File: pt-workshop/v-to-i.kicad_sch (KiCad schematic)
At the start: 12 parts, among them Q301 NST65011, U301 TL972

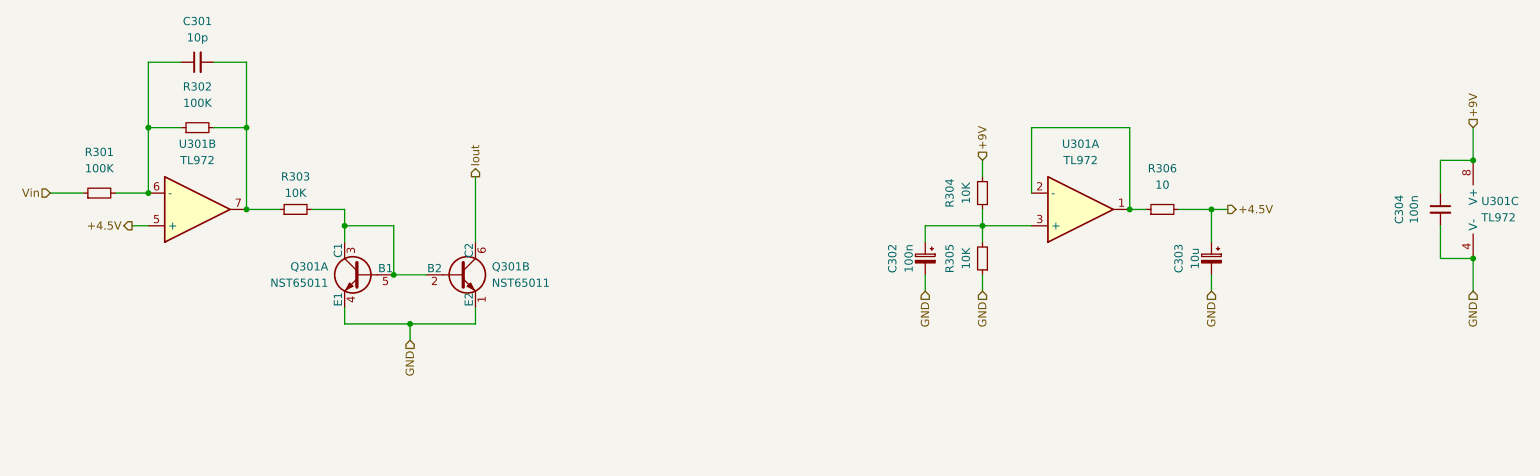
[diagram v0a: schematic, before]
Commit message: 10 pin socket
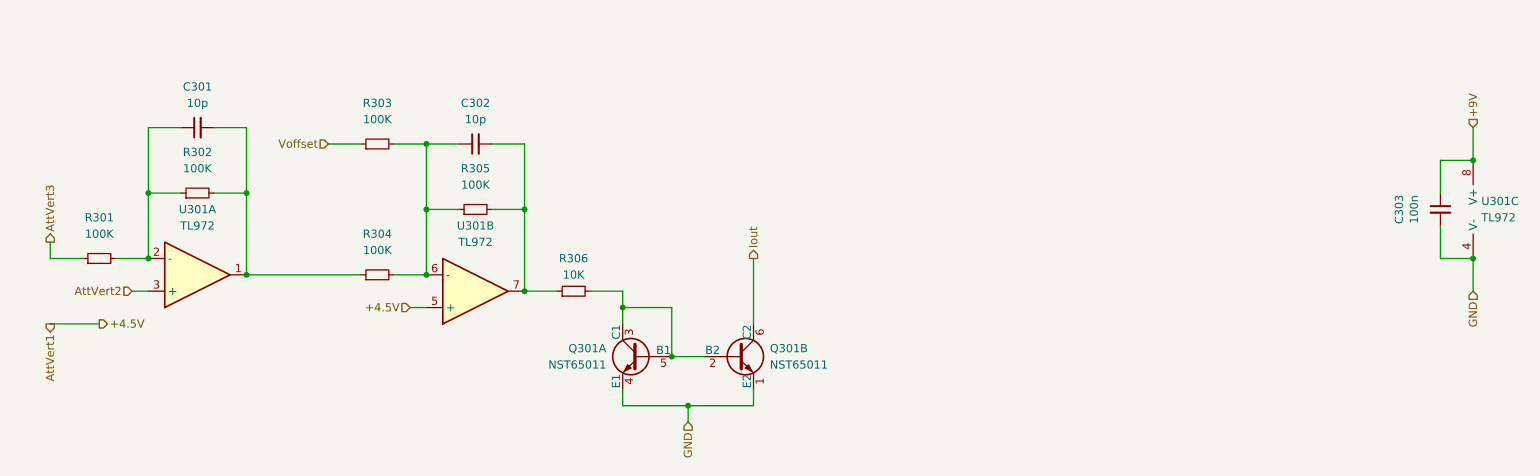
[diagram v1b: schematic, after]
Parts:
- removed C302: 100n, Capacitor_SMD:CP_Elec_4x5.4, symbol Device:C_Polarized_Small
- removed C303: 10u, Capacitor_SMD:CP_Elec_5x5.4, symbol Device:C_Polarized_Small
- removed R305: 10K, Resistor_SMD:R_0603_1608Metric_Pad0.98x0.95mm_HandSolder, symbol Device:R_Small
- removed R306: 10, Resistor_SMD:R_0603_1608Metric_Pad0.98x0.95mm_HandSolder, symbol Device:R_Small
- added C301: 10p, Capacitor_SMD:C_0603_1608Metric_Pad1.08x0.95mm_HandSolder, symbol Device:C_Small
- added R301, R302: 100K, Resistor_SMD:R_0603_1608Metric_Pad0.98x0.95mm_HandSolder, symbol Device:R_Small
- R304: value 10K -> 100K; LCSC C98220 -> (none); Mouser 603-RT0603DRE1010KL -> (none)
- renumbered C301 to C302, C304 to C303, R301 to R303, R302 to R305, R303 to R306
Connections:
- net +9V: no longer R304.2
- net at U301.2 (-): now also C301.1, R301.2, R302.1; no longer U301.1
- net at C302.1, R303.2, R305.1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: now also R304.2
- net at R304.1: now also U301.1, C301.2, R302.2; no longer U301.3 (+)
- net Vin renamed Voffset
- new net AttVert2: U301.3 (+)
- new net AttVert3: R301.1
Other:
- moved on the sheet: C302, Q301A, Q301B, R303, R305, R306, U301A, U301B

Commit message: Mapped components
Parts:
- added TP1: Vatt, TestPoint:TestPoint_Pad_1.5x1.5mm, symbol Connector:TestPoint
- added TP2: Vd, TestPoint:TestPoint_Pad_1.5x1.5mm, symbol Connector:TestPoint
- C301, C302: LCSC (none) -> C91367
- C303: LCSC C497032 -> C57112
- R301, R302, R303, R304, R305: LCSC (none) -> C25803
- R306: LCSC C98220 -> C25804
- U301: LCSC (none) -> C46127
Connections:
- net at C302.2, R305.2, R306.1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: now also TP2.1
- net at C301.2, R302.2, R304.1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: now also TP1.1
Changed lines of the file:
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@@
   (junction (at 91.44 53.34) (diameter 0) (color 0 0 0 0)
   )
+  (junction (at 71.12 53.34) (diameter 0) (color 0 0 0 0)
+  )
   (junction (at 48.26 40.64) (diameter 0) (color 0 0 0 0)
   )
@@
     (stroke (width 0) (type default) (color 0 0 0 0))
   )
+  (wire (pts (xy 71.12 53.34) (xy 81.28 53.34))
+    (stroke (width 0) (type default) (color 0 0 0 0))
+  )
   (wire (pts (xy 91.44 33.02) (xy 91.44 43.18))
     (stroke (width 0) (type default) (color 0 0 0 0))
@@
     (stroke (width 0) (type default) (color 0 0 0 0))
   )
-  (wire (pts (xy 63.5 53.34) (xy 81.28 53.34))
+  (wire (pts (xy 63.5 53.34) (xy 71.12 53.34))
     (stroke (width 0) (type default) (color 0 0 0 0))
   )
@@
     (stroke (width 0) (type default) (color 0 0 0 0))
   )
+  (wire (pts (xy 71.12 53.34) (xy 71.12 59.69))
+    (stroke (width 0) (type default) (color 0 0 0 0))
+  )
   (wire (pts (xy 106.68 55.88) (xy 111.76 55.88))
+    (stroke (width 0) (type default) (color 0 0 0 0))
+  )
+  (wire (pts (xy 106.68 55.88) (xy 106.68 58.42))
     (stroke (width 0) (type default) (color 0 0 0 0))
   )
@@
       (effects (font (size 1.27 1.27)) hide)
     )
-    (property "LCSC" "C497032" (id 4) (at 248.92 43.18 0)
+    (property "LCSC" "C57112" (id 4) (at 248.92 43.18 0)
       (effects (font (size 1.27 1.27)) hide)
     )
@@
       (effects (font (size 1.27 1.27)) hide)
     )
+    (property "LCSC" "C25803" (id 4) (at 40.64 50.8 0)
+      (effects (font (size 1.27 1.27)) hide)
+    )
     (pin "1")
     (pin "2")
@@
     )
     (property "Datasheet" "~" (id 3) (at 256.54 43.18 0)
+      (effects (font (size 1.27 1.27)) hide)
+    )
+    (property "LCSC" "C46127" (id 4) (at 256.54 43.18 0)
       (effects (font (size 1.27 1.27)) hide)
     )
@@
       (effects (font (size 1.27 1.27)) hide)
     )
-    (pin "1")
-    (pin "2")
+    (property "LCSC" "C91367" (id 4) (at 99.06 33.02 0)
+      (effects (font (size 1.27 1.27)) hide)
+    )
+    (pin "1")
+    (pin "2")
+  )
+  (symbol (lib_id "Connector:TestPoint") (at 71.12 59.69 180) (unit 1)
+    (in_bom yes) (on_board yes) (fields_autoplaced)
+    (property "Reference" "TP1" (id 0) (at 73.66 61.7219 0)
+      (effects (font (size 1.27 1.27)) (justify right))
+    )
+    (property "Value" "Vatt" (id 1) (at 73.66 64.2619 0)
+      (effects (font (size 1.27 1.27)) (justify right))
+    )
+    (property "Footprint" "TestPoint:TestPoint_Pad_1.5x1.5mm" (id 2) (at 66.04 59.69 0)
+      (effects (font (size 1.27 1.27)) hide)
+    )
+    (property "Datasheet" "~" (id 3) (at 66.04 59.69 0)
+      (effects (font (size 1.27 1.27)) hide)
+    )
+    (pin "1")
   )
   (symbol (lib_id "Device:R_Small") (at 55.88 40.64 90) (unit 1)
@@
       (effects (font (size 1.27 1.27)) hide)
     )
+    (property "LCSC" "C25803" (id 4) (at 55.88 40.64 0)
+      (effects (font (size 1.27 1.27)) hide)
+    )
     (pin "1")
     (pin "2")
@@
     )
     (property "Datasheet" "~" (id 3) (at 83.82 53.34 0)
+      (effects (font (size 1.27 1.27)) hide)
+    )
+    (property "LCSC" "C25803" (id 4) (at 83.82 53.34 0)
       (effects (font (size 1.27 1.27)) hide)
     )
@@
       (effects (font (size 1.27 1.27)) hide)
     )
-    (property "LCSC" "C98220" (id 4) (at 114.3 55.88 0)
+    (property "LCSC" "C25804" (id 4) (at 114.3 55.88 0)
       (effects (font (size 1.27 1.27)) hide)
     )
@@
     )
     (property "Datasheet" "~" (id 3) (at 55.88 53.34 0)
+      (effects (font (size 1.27 1.27)) hide)
+    )
+    (property "LCSC" "C46127" (id 4) (at 55.88 53.34 0)
       (effects (font (size 1.27 1.27)) hide)
     )
@@
       (effects (font (size 1.27 1.27)) hide)
     )
+    (property "LCSC" "C46127" (id 4) (at 99.06 55.88 0)
+      (effects (font (size 1.27 1.27)) hide)
+    )
     (pin "1")
     (pin "2")
@@
       (effects (font (size 1.27 1.27)) hide)
     )
-    (pin "1")
-    (pin "2")
+    (property "LCSC" "C91367" (id 4) (at 55.88 30.48 0)
+      (effects (font (size 1.27 1.27)) hide)
+    )
+    (pin "1")
+    (pin "2")
+  )
+  (symbol (lib_id "Connector:TestPoint") (at 106.68 58.42 180) (unit 1)
+    (in_bom yes) (on_board yes) (fields_autoplaced)
+    (property "Reference" "TP2" (id 0) (at 109.22 60.4519 0)
+      (effects (font (size 1.27 1.27)) (justify right))
+    )
+    (property "Value" "Vd" (id 1) (at 109.22 62.9919 0)
+      (effects (font (size 1.27 1.27)) (justify right))
+    )
+    (property "Footprint" "TestPoint:TestPoint_Pad_1.5x1.5mm" (id 2) (at 101.6 58.42 0)
+      (effects (font (size 1.27 1.27)) hide)
+    )
+    (property "Datasheet" "~" (id 3) (at 101.6 58.42 0)
+      (effects (font (size 1.27 1.27)) hide)
+    )
+    (pin "1")
   )
   (symbol (lib_id "Device:R_Small") (at 99.06 43.18 90) (unit 1)
@@
       (effects (font (size 1.27 1.27)) hide)
     )
+    (property "LCSC" "C25803" (id 4) (at 99.06 43.18 0)
+      (effects (font (size 1.27 1.27)) hide)
+    )
     (pin "1")
     (pin "2")
@@
       (effects (font (size 1.27 1.27)) hide)
     )
+    (property "LCSC" "C25803" (id 4) (at 83.82 33.02 0)
+      (effects (font (size 1.27 1.27)) hide)
+    )

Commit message: v1rev1?
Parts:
- Q301: LCSC (none) -> C463185
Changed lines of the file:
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@@
+      (effects (font (size 1.27 1.27)) hide)
+    )
+    (property "LCSC" "C463185" (id 4) (at 124.46 66.04 0)
       (effects (font (size 1.27 1.27)) hide)
     )
@@
       (effects (font (size 1.27 1.27)) hide)
     )
+    (property "LCSC" "C463185" (id 4) (at 139.7 66.04 0)
+      (effects (font (size 1.27 1.27)) hide)
+    )

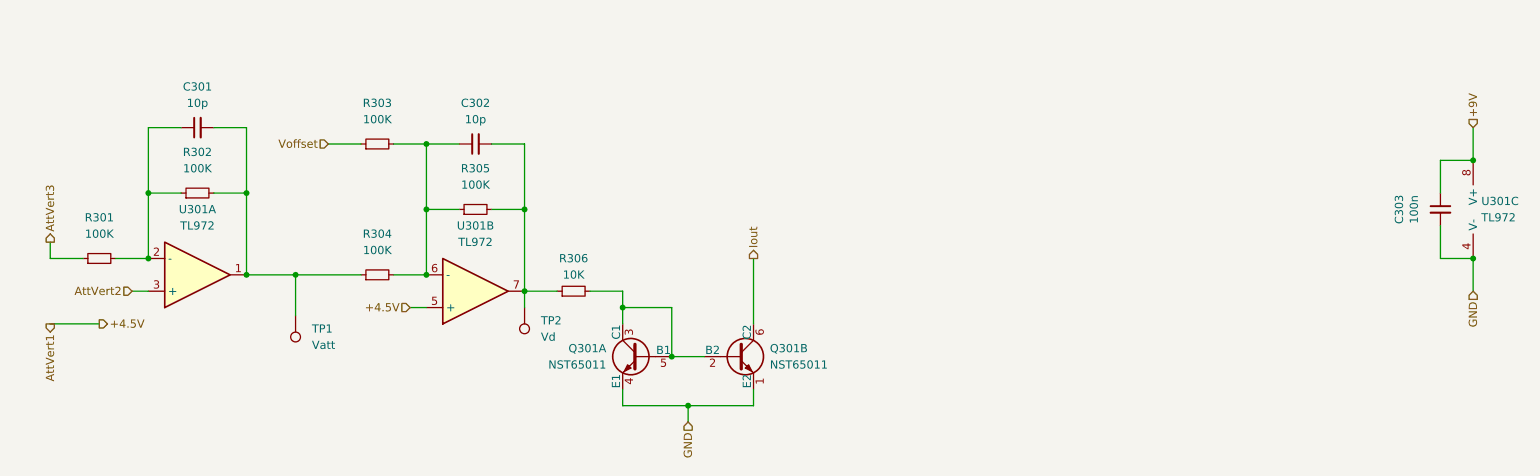
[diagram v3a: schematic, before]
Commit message: PTT without attverts
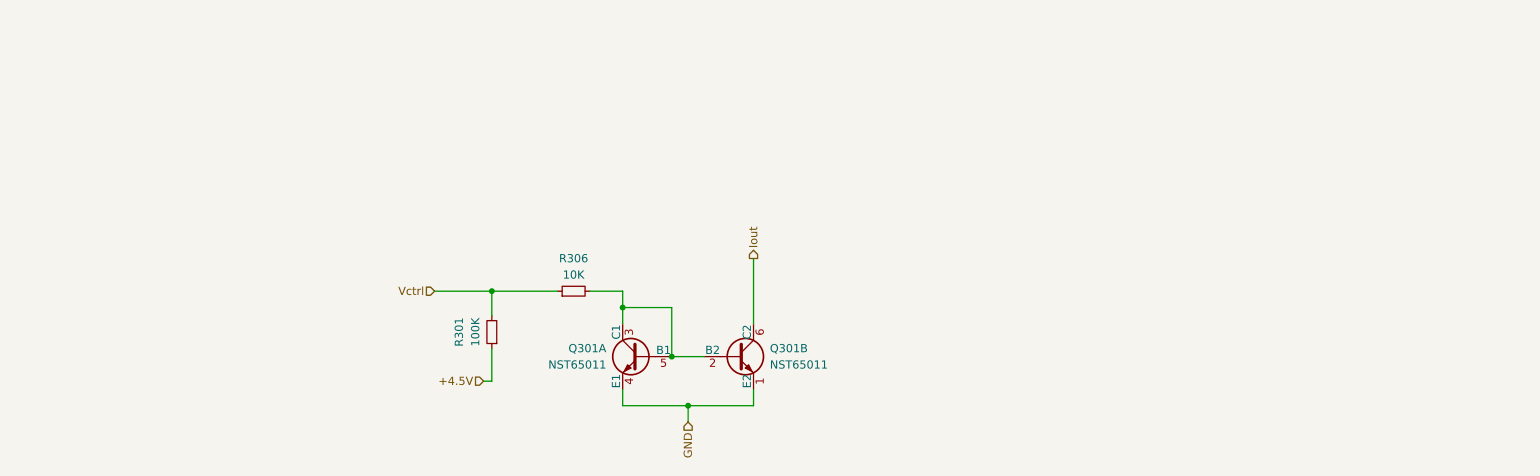
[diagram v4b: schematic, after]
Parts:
- removed C301, C302: 10p, Capacitor_SMD:C_0603_1608Metric_Pad1.08x0.95mm_HandSolder, symbol Device:C_Small
- removed C303: 100n, Capacitor_SMD:C_0603_1608Metric_Pad1.08x0.95mm_HandSolder, symbol Device:C_Small
- removed R302, R303, R304, R305: 100K, Resistor_SMD:R_0603_1608Metric_Pad0.98x0.95mm_HandSolder, symbol Device:R_Small
- removed TP1: Vatt, TestPoint:TestPoint_Pad_1.5x1.5mm, symbol Connector:TestPoint
- removed TP2: Vd, TestPoint:TestPoint_Pad_1.5x1.5mm, symbol Connector:TestPoint
- removed U301: TL972, Package_SO:SOIC-8_3.9x4.9mm_P1.27mm, symbol Device:Opamp_Dual
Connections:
- net AttVert3 is gone; now on net +4.5V: R301.1
- net Vctrl: now reaches R301.2
- net Vctrl: now also R306.1

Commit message: jlc
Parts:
- R306: Mouser 603-RT0603DRE1010KL -> (none)
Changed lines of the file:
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@@
       (effects (font (size 1.27 1.27)) hide)
     )
-    (property "Mouser" "603-RT0603DRE1010KL" (id 5) (at 114.3 55.88 0)
+    (property "Mouser" "" (id 5) (at 114.3 55.88 0)
       (effects (font (size 1.27 1.27)) hide)
     )

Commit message: PTT schem export
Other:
- company: (none) -> Pedal Markt
- title: (none) -> PTT
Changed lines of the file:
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@@
 (kicad_sch (version 20211123) (generator eeschema)
   (paper "A4")
+  (title_block
+    (title "PTT")
+    (date "2024-05-11")
+    (rev "v1rev2")
+    (company "Pedal Markt")
+    (comment 1 "Andrey Salomatin")
+  )
   (junction (at 101.6 55.88) (diameter 0) (color 0 0 0 0)
   )

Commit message: wip
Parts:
- Q301: value NST65011 -> MMDT3904; LCSC C463185 -> C41375125; LCSC v0 (none) -> C463185
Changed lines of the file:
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@@
     (title "PTT")
     (date "2024-05-11")
-    (rev "v1rev2")
+    (rev "v1rev3")
     (company "Pedal Markt")
     (comment 1 "Andrey Salomatin")
@@
       (effects (font (size 1.27 1.27)) (justify left))
     )
-    (property "Value" "NST65011" (id 1) (at 119.38 67.3099 0)
+    (property "Value" "MMDT3904" (id 1) (at 119.38 67.3099 0)
       (effects (font (size 1.27 1.27)) (justify left))
     )
@@
       (effects (font (size 1.27 1.27)) hide)
     )
-    (property "LCSC" "C463185" (id 4) (at 124.46 66.04 0)
+    (property "LCSC" "C41375125" (id 4) (at 124.46 66.04 0)
+      (effects (font (size 1.27 1.27)) hide)
+    )
+    (property "LCSC v0" "C463185" (id 5) (at 124.46 66.04 0)
       (effects (font (size 1.27 1.27)) hide)
     )
@@
       (effects (font (size 1.27 1.27)) (justify left))
     )
-    (property "Value" "NST65011" (id 1) (at 144.78 67.3099 0)
+    (property "Value" "MMDT3904" (id 1) (at 144.78 67.3099 0)
       (effects (font (size 1.27 1.27)) (justify left))
     )
@@
       (effects (font (size 1.27 1.27)) hide)
     )
-    (property "LCSC" "C463185" (id 4) (at 139.7 66.04 0)
+    (property "LCSC" "C41375125" (id 4) (at 139.7 66.04 0)
       (effects (font (size 1.27 1.27)) hide)
     )
+    (property "LCSC v0" "C463185" (id 5) (at 139.7 66.04 0)
+      (effects (font (size 1.27 1.27)) hide)
+    )
